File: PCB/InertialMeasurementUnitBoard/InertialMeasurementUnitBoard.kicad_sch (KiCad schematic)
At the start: 3 parts, among them X1 32.768 kHz

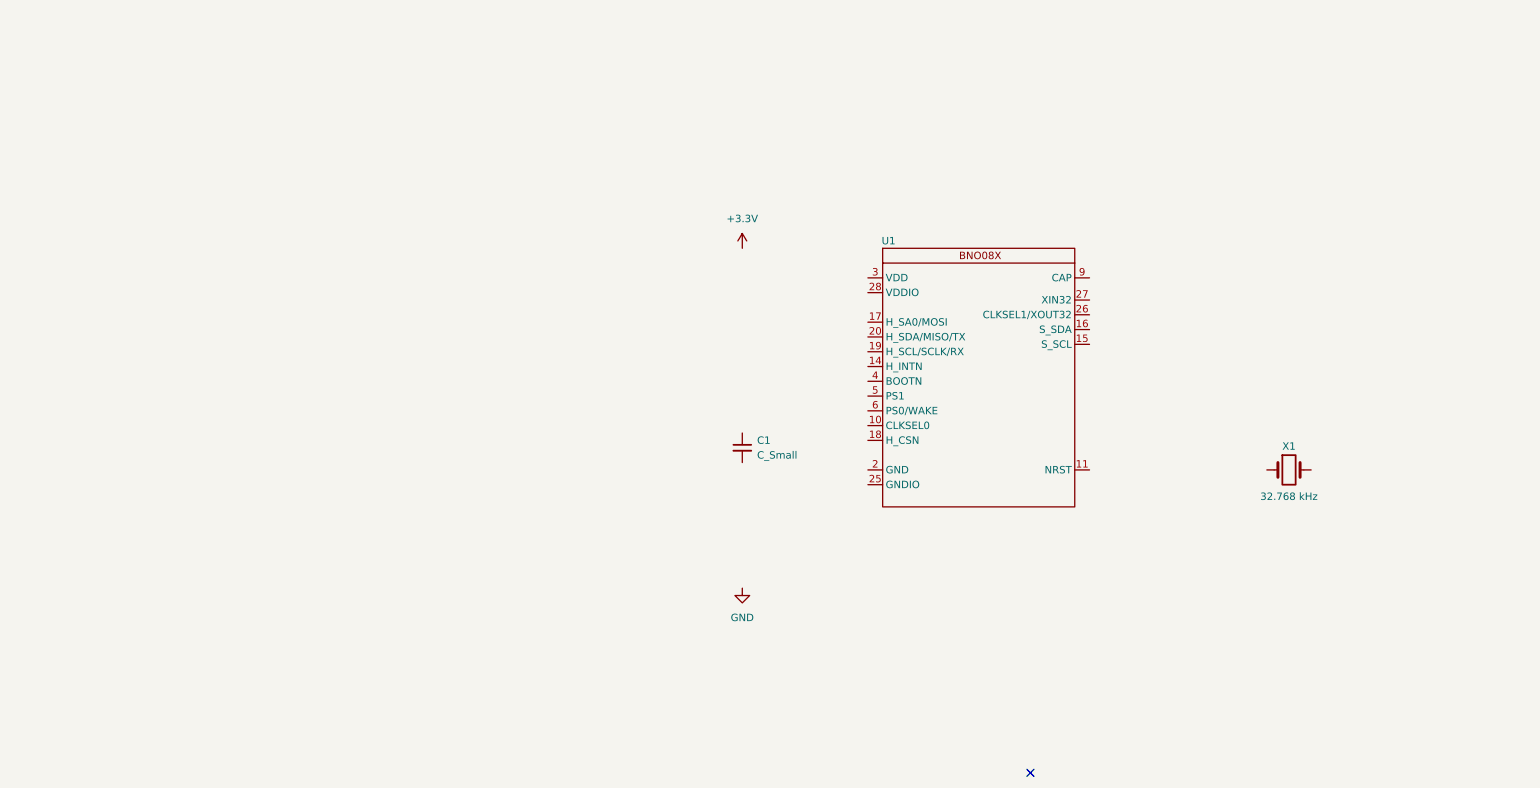
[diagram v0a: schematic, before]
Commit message: Initial work on IMU board
Some configuration work done; added power LED
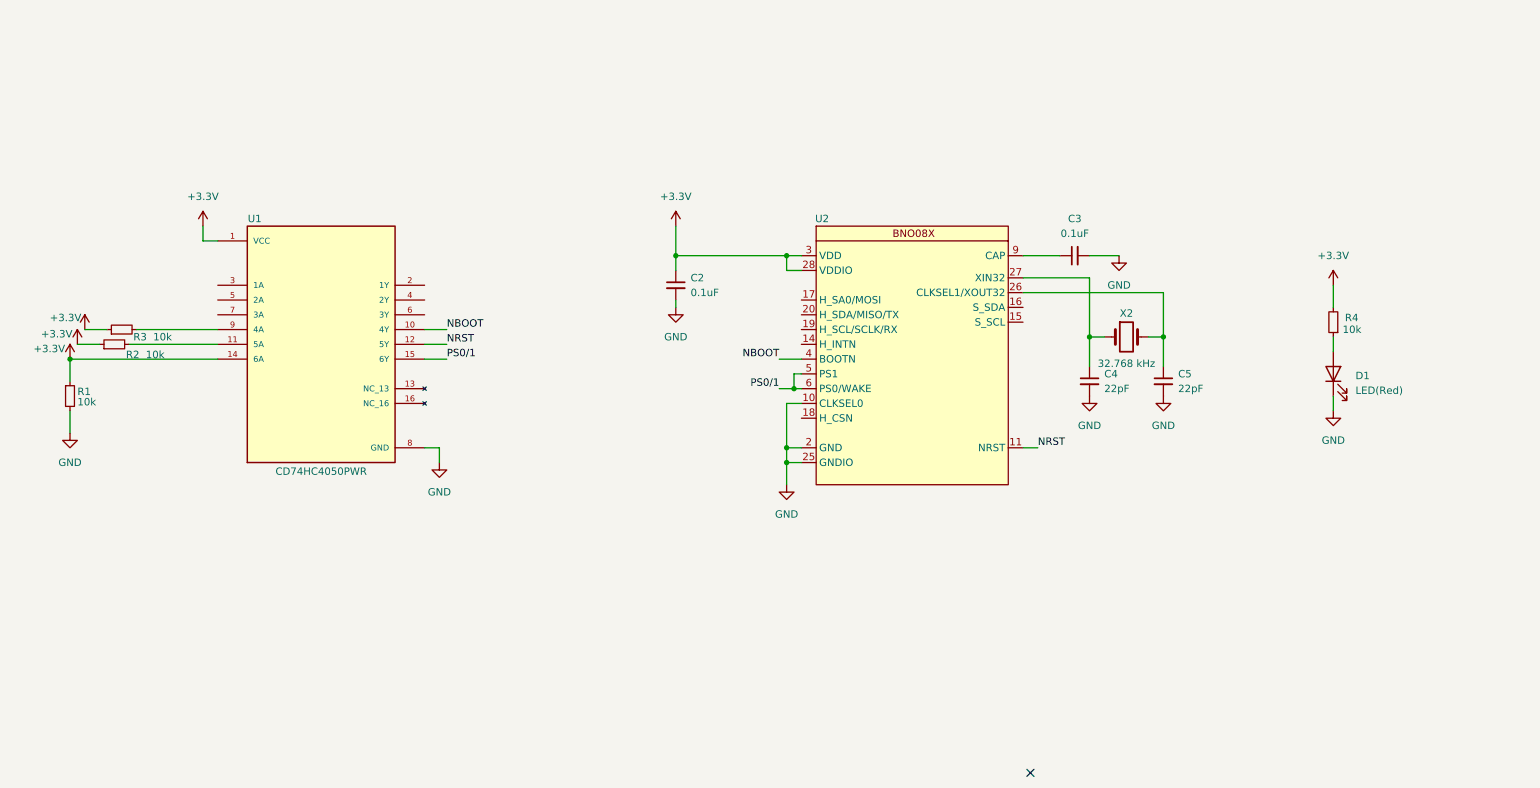
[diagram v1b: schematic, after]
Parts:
- removed C1: C_Small, symbol Device:C_Small
- removed U1: ~, symbol Customs:BNO08X
- removed X1: 32.768 kHz, symbol Device:Crystal
- added C2, C3: 0.1uF, symbol Device:C_Small
- added C4, C5: 22pF, symbol Device:C_Small
- added D1: LED(Red), symbol Device:LED
- added R1, R2, R3, R4: 10k, symbol Device:R_Small
- added U1: CD74HC4050PWR, CD74HC4050PWR:SOP65P640X120-16N, symbol CD74HC4050PWR:CD74HC4050PWR
- added U2: ~, symbol 445Symbols:BNO08X
- added X2: 32.768 kHz, symbol Device:Crystal
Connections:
- net +3.3V: now also C2.1, R1.1, R2.1, R3.1, R4.2, U1.1 (VCC), U1.14 (6A), U2.28 (VDDIO), U2.3 (VDD)
- net GND: now also C2.2, C3.2, C4.2, C5.2, D1.1 (K), R1.2, U1.8 (GND), U2.10 (CLKSEL0), U2.2 (GND), U2.25 (GNDIO)
- new net: C5.1, U2.26 (CLKSEL1/XOUT32), X2.2
- new net: C4.1, U2.27 (XIN32), X2.1
- new net: C3.1, U2.9 (CAP)
- new net: R2.2, U1.11 (5A)
- new net: R3.2, U1.9 (4A)
- new net: D1.2 (A), R4.1
- new net NBOOT: U1.10 (4Y), U2.4 (BOOTN)
- new net NRST: U1.12 (5Y), U2.11 (NRST)
- new net PS0/1: U1.15 (6Y), U2.5 (PS1), U2.6 (PS0/WAKE)

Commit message: Finish IMU schematic
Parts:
- added R5: 10k, Resistor_SMD:R_0805_2012Metric_Pad1.20x1.40mm_HandSolder, symbol Device:R_Small
- C2, C3: footprint (none) -> Capacitor_SMD:C_0805_2012Metric_Pad1.18x1.45mm_HandSolder
- C4, C5: footprint (none) -> Capacitor_SMD:C_0603_1608Metric_Pad1.08x0.95mm_HandSolder
- D1: footprint (none) -> LED_SMD:LED_0603_1608Metric_Pad1.05x0.95mm_HandSolder
- R1, R2, R3, R4: footprint (none) -> Resistor_SMD:R_0805_2012Metric_Pad1.20x1.40mm_HandSolder
- U2: footprint (none) -> BNO085:IC_BNO080
- X2: footprint (none) -> Oscillator:Oscillator_SMD_Fordahl_DFAS15-4Pin_5.0x3.2mm_HandSoldering
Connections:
- net GND: now also R5.1
- net INT_N: now reaches U2.14 (H_INTN)
- net MOSI: now reaches U2.17 (H_SA0/MOSI)
- net CS_N: now reaches U2.18 (H_CSN)
- net CS_N: now also U1.6 (3Y)
- net SCLK: now reaches U2.19 (H_SCL/SCLK/RX)
- net MISO: now reaches U2.20 (H_SDA/MISO/TX)
- net at U1.7 (3A): now also R5.2
- net NBOOT renamed BOOT_N
- net NRST renamed RST_N

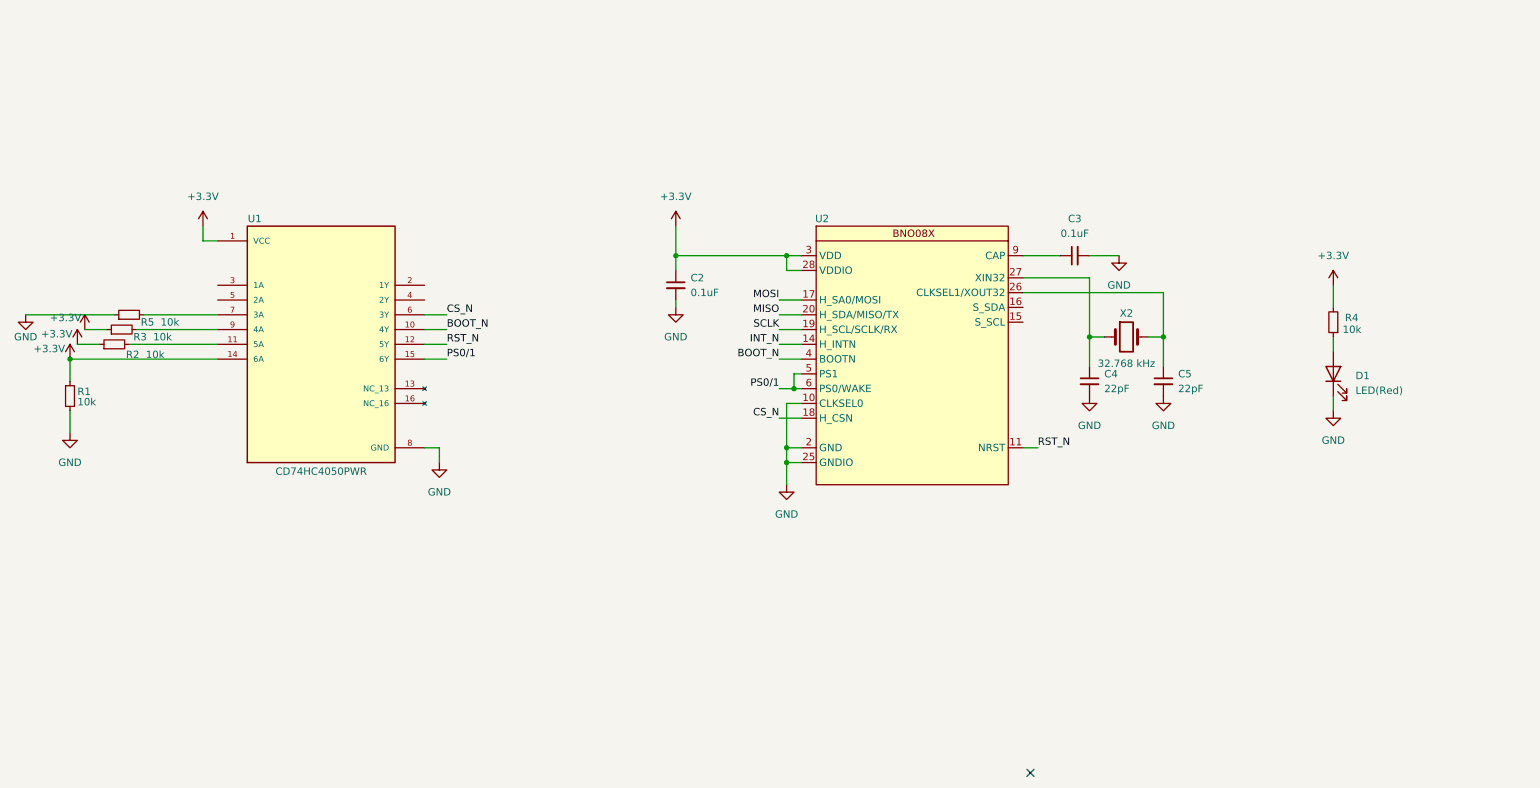
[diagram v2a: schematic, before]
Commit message: 2/29 IMU Board
Added connectors to schematic, started layout
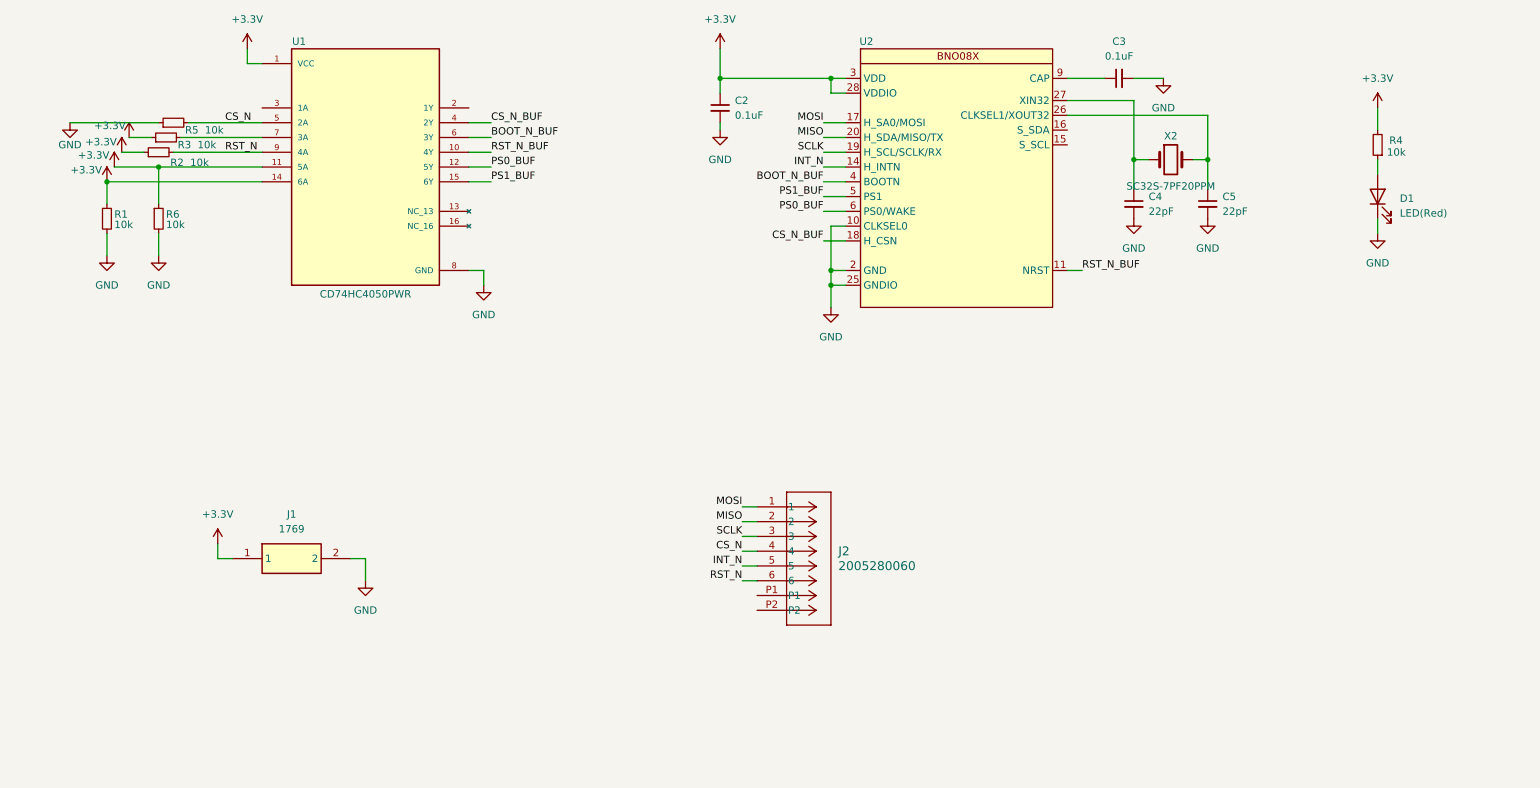
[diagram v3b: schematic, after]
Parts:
- added J1: 1769, Adafruit Accessories JST-PH 2-pin SMT Right Angle Connect:1769, symbol Adafruit Accessories JST-PH 2-pin SMT Right Angle Connect:1769
- added J2: 2005280060, WM24188TR-ND:CON_2005280060_MOL, symbol WM24188TR-ND:2005280060
- added R6: 10k, Resistor_SMD:R_0805_2012Metric_Pad1.20x1.40mm_HandSolder, symbol Device:R_Small
- X2: value 32.768 kHz -> SC32S-7PF20PPM; footprint Oscillator:Oscillator_SMD_Fordahl_DFAS15-4Pin_5.0x3.2mm_HandSoldering -> SC32S-7PF20PPM:XTAL_SC32S-7PF20PPM_EPS
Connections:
- net +3.3V: now also U1.11 (5A), J1.1, R6.1
- net CS_N: now also R5.2, U1.5 (2A), J2.4; no longer U1.6 (3Y), U2.18 (H_CSN)
- net GND: now also J1.2, R6.2
- net INT_N: now also J2.5
- net MISO: now also J2.2
- net MOSI: now also J2.1
- net RST_N: now also R2.2, U1.9 (4A), J2.6; no longer U1.12 (5Y), U2.11 (NRST)
- net SCLK: now also J2.3
- net CS_N_BUF: now reaches U1.4 (2Y)
- net CS_N_BUF: now also U2.18 (H_CSN)
- net at U1.7 (3A): now also R3.2; no longer R5.2
- net BOOT_N renamed BOOT_N_BUF
- net BOOT_N_BUF: now also U1.6 (3Y); no longer U1.10 (4Y)
- net PS0/1 renamed PS1_BUF
- net PS1_BUF: no longer U2.6 (PS0/WAKE)
- new net PS0_BUF: U1.12 (5Y), U2.6 (PS0/WAKE)
- new net RST_N_BUF: U1.10 (4Y), U2.11 (NRST)
- no-connect marks 1 -> 0
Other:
- moved on the sheet: C2, C3, C4, C5, D1, R1, R2, R3, R4, R5, U1, U2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

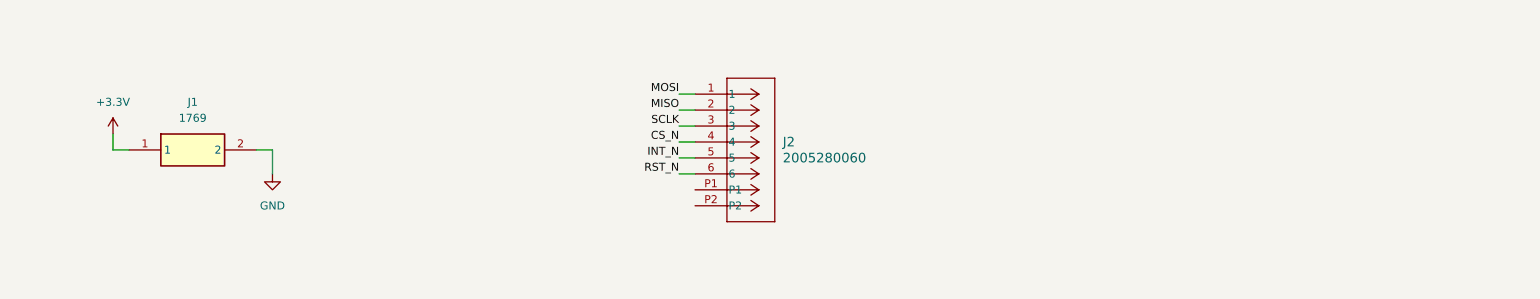
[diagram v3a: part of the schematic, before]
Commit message: Initial completion of Inertial Measurement Unit Board
Add test points for BMS outputs, complete layout.
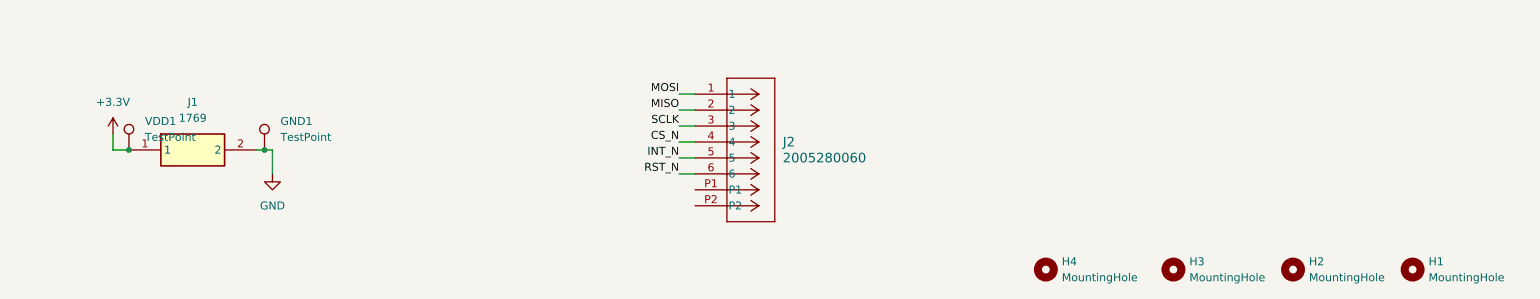
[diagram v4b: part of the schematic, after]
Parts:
- added GND1, VDD1: TestPoint, TestPoint:TestPoint_THTPad_D2.0mm_Drill1.0mm, symbol Connector:TestPoint
- added H1, H2, H3, H4: MountingHole, MountingHole:MountingHole_3.2mm_M3, symbol Mechanical:MountingHole
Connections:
- net +3.3V: now also VDD1.1
- net GND: now also GND1.1
